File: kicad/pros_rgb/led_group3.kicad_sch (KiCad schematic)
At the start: 3 parts

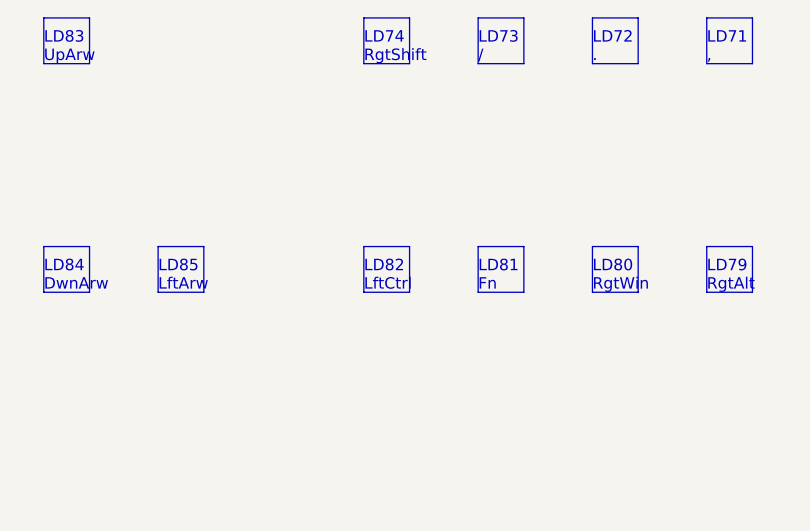
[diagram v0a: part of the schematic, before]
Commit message: kicad/pros_rgb: fix typos
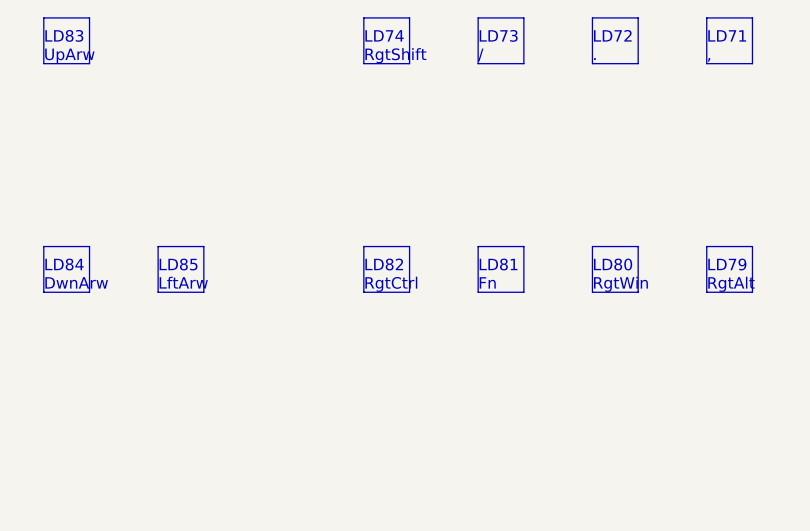
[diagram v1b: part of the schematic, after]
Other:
- note added: "LD82 RgtCtrl"
- note removed: "LD82 LftCtrl"
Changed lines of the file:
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@@
     (effects (font (size 1.27 1.27)) (justify left bottom))
   )
-  (text "LD82\nLftCtrl" (at 106.68 156.21 0)
+  (text "LD82\nRgtCtrl" (at 106.68 156.21 0)
     (effects (font (size 1.27 1.27)) (justify left bottom))
   )

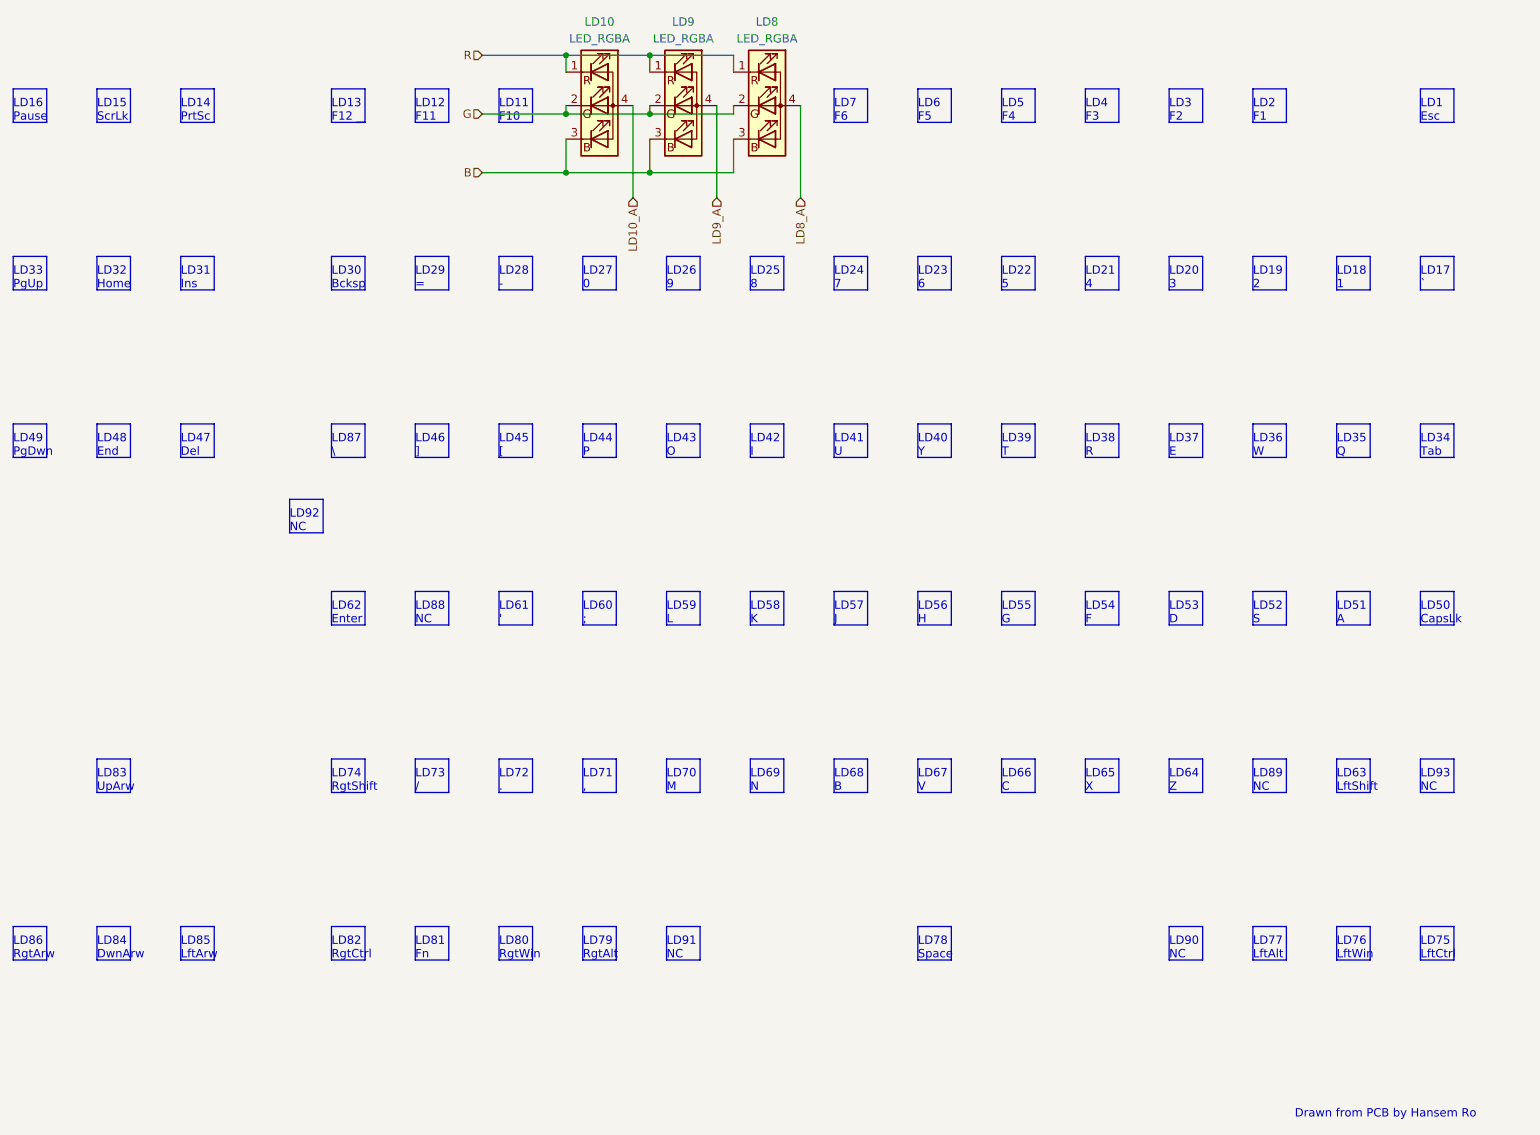
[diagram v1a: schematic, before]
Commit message: kicad/pros_rgb: order led groups by channel number
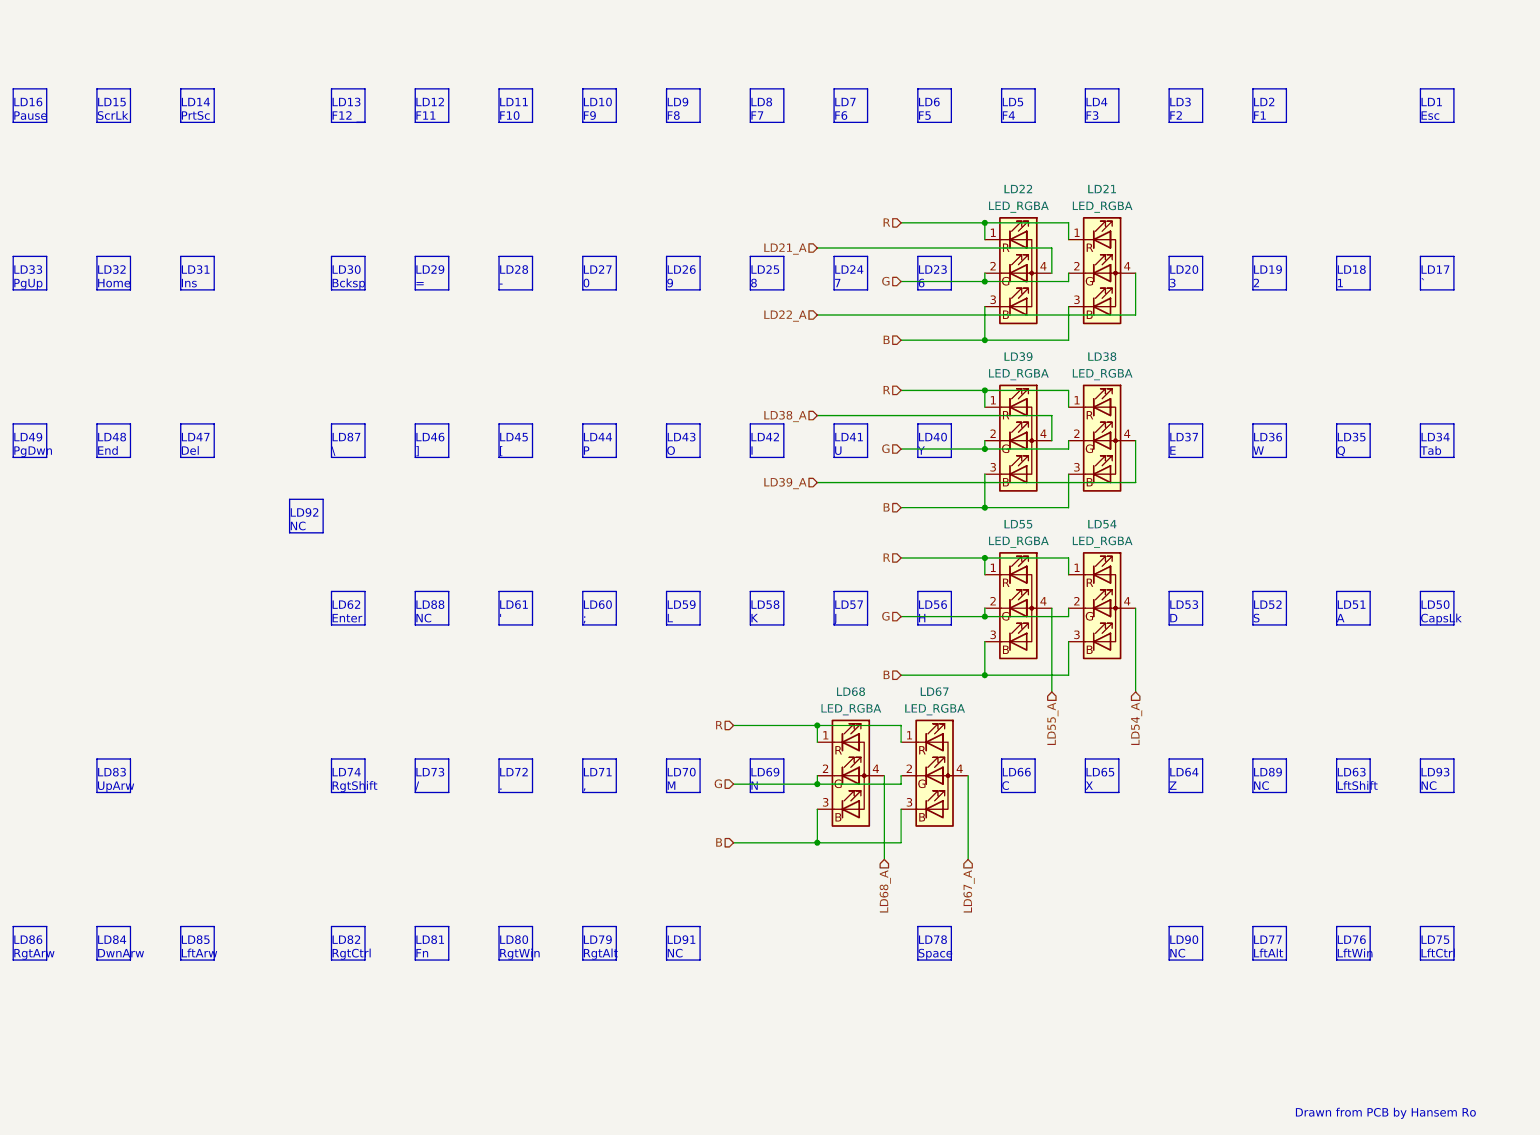
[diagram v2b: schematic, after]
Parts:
- removed LD10, LD8, LD9: LED_RGBA, symbol Device:LED_RGBA
- added LD21, LD22, LD38, LD39, LD54, LD55, LD67, LD68: LED_RGBA, symbol Device:LED_RGBA
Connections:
- net B: now also LD21.3 (BK), LD22.3 (BK), LD38.3 (BK), LD39.3 (BK), LD54.3 (BK), LD55.3 (BK), LD67.3 (BK), LD68.3 (BK)
- net G: now also LD21.2 (GK), LD22.2 (GK), LD38.2 (GK), LD39.2 (GK), LD54.2 (GK), LD55.2 (GK), LD67.2 (GK), LD68.2 (GK)
- net R: now also LD21.1 (RK), LD22.1 (RK), LD38.1 (RK), LD39.1 (RK), LD54.1 (RK), LD55.1 (RK), LD67.1 (RK), LD68.1 (RK)
- new net LD21_A: LD22.4 (A)
- new net LD22_A: LD21.4 (A)
- new net LD38_A: LD39.4 (A)
- new net LD39_A: LD38.4 (A)
- new net LD54_A: LD54.4 (A)
- new net LD55_A: LD55.4 (A)
- new net LD67_A: LD67.4 (A)
- new net LD68_A: LD68.4 (A)
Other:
- note added: "LD10 F9"
- note added: "LD8 F7"
- note added: "LD9 F8"
- note removed: "LD21 4"
- note removed: "LD22 5"
- note removed: "LD38 R"
- note removed: "LD39 T"
- note removed: "LD54 F"
- note removed: "LD55 G"
- note removed: "LD67 V"
- note removed: "LD68 B"
